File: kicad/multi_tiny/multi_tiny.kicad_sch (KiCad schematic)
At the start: 43 parts, among them J1 Conn_02x04, J2 Conn_02x03_Odd_Even, J3 Conn_01x13, J4 Conn_02x14_Odd_Even, SW1 SW_SPDT, SW2 SW_SPDT, SW3 SW_SPDT, SW4 SW_SPST, U1 CD4052B, U2 CD4052B, U3 CD4052B, U4 CD4052B

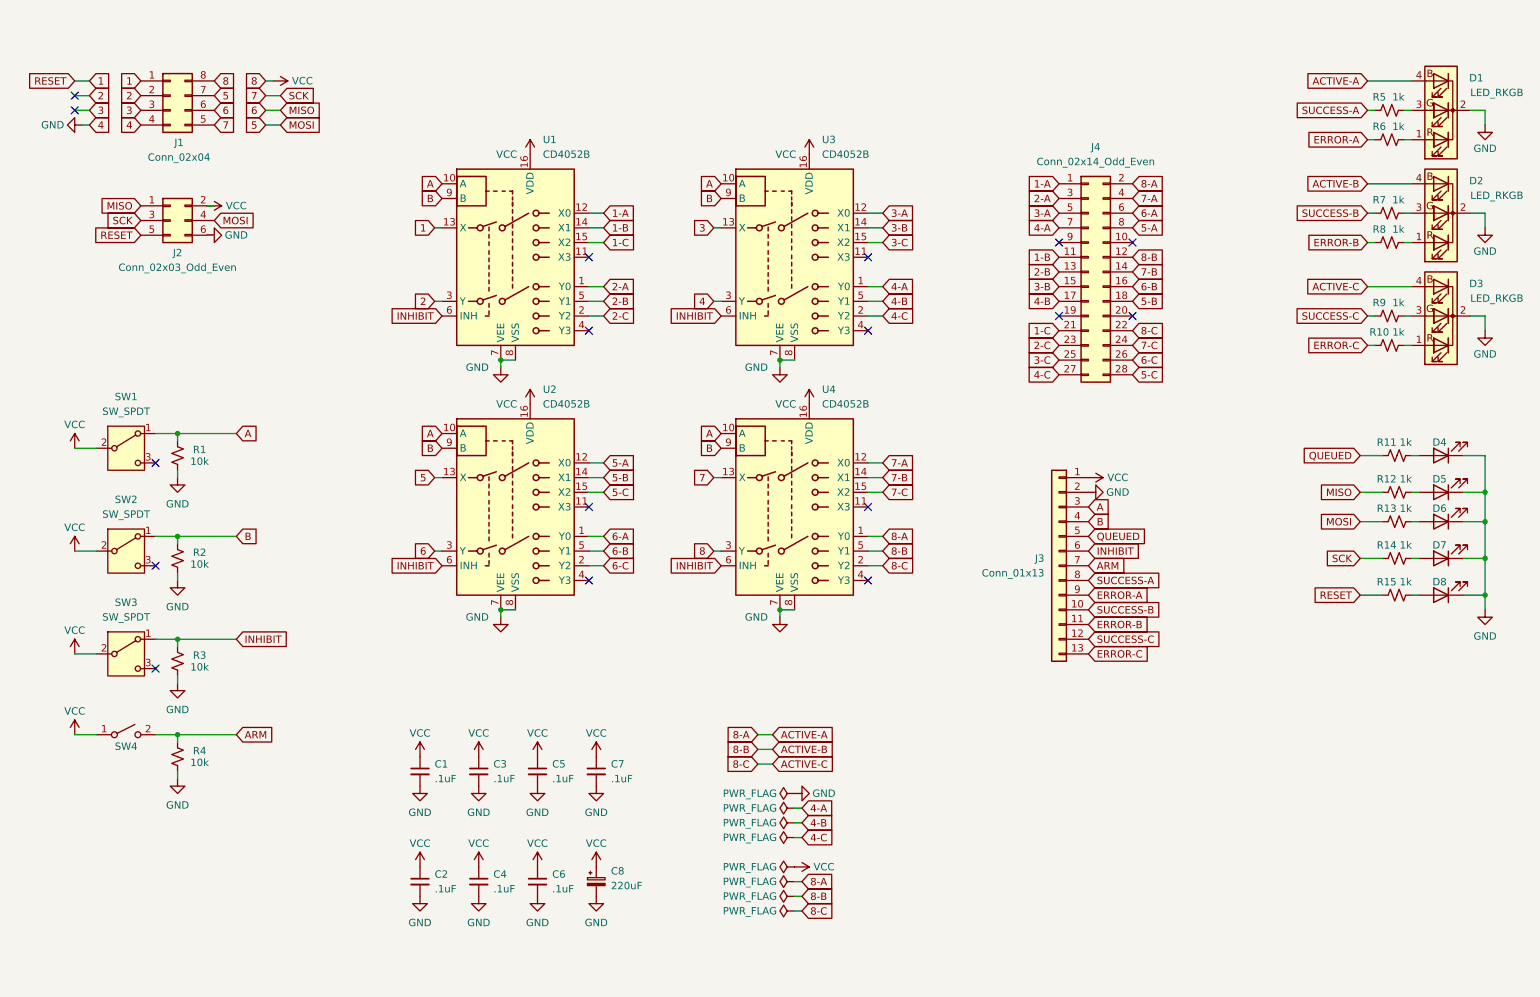
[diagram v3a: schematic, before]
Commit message: Add more IO and organize
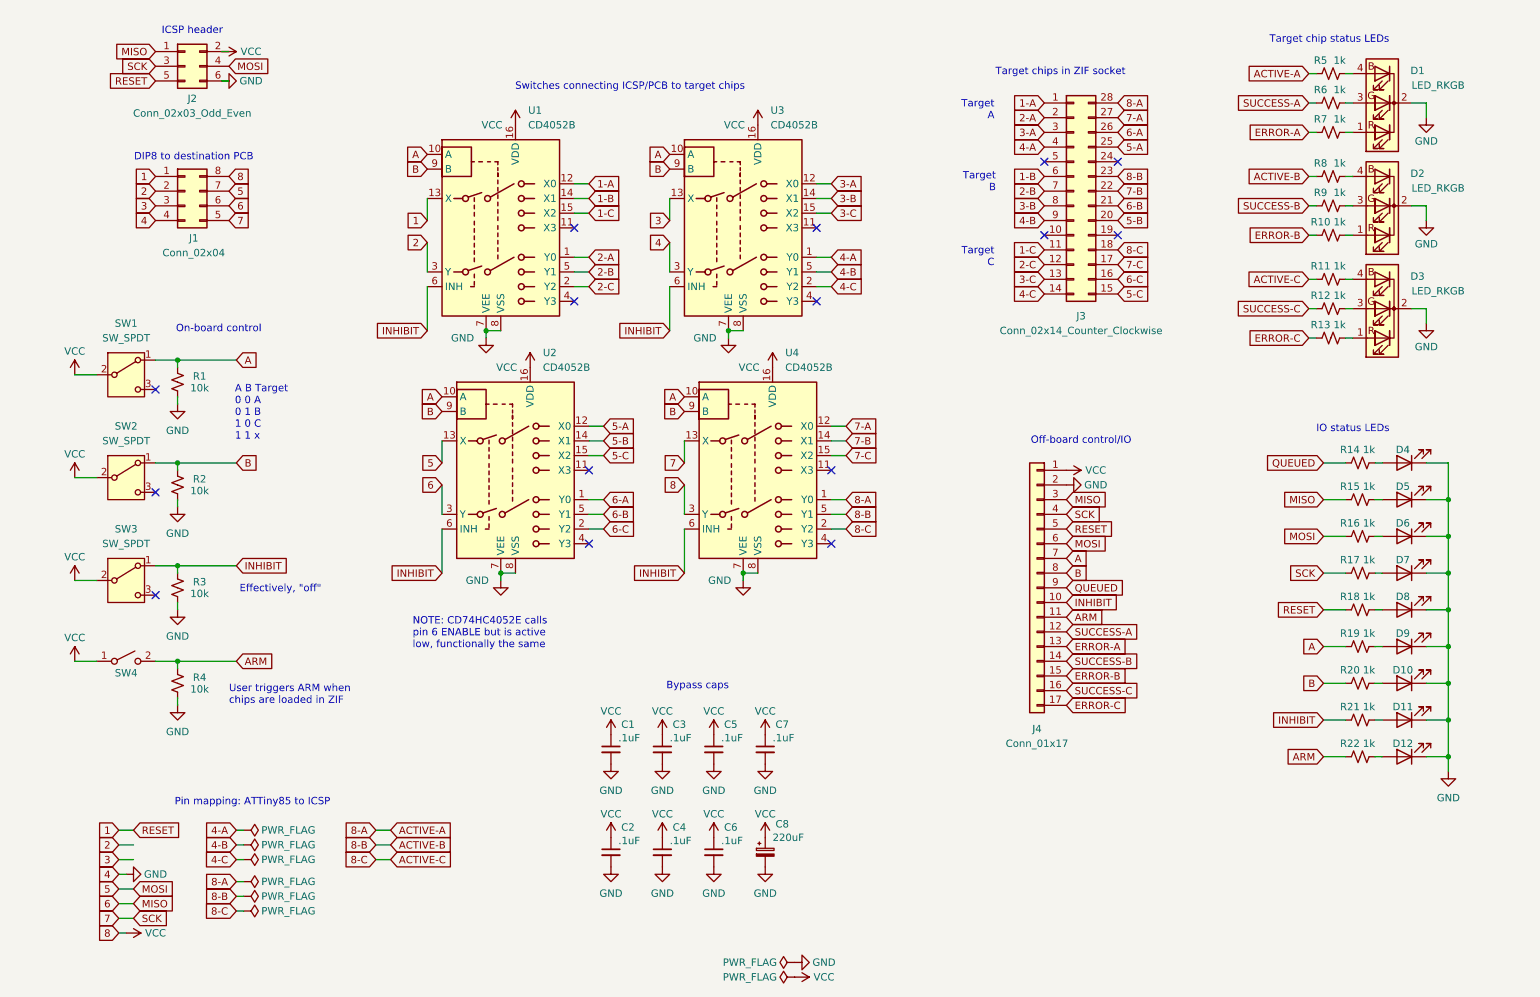
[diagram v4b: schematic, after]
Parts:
- removed J3: Conn_01x13, symbol Connector_Generic:Conn_01x13
- removed J4: Conn_02x14_Odd_Even, symbol Connector_Generic:Conn_02x14_Odd_Even
- added D10, D11, D12, D9: LED, symbol Device:LED
- added J3: Conn_02x14_Counter_Clockwise, symbol Connector_Generic:Conn_02x14_Counter_Clockwise
- added J4: Conn_01x17, symbol Connector_Generic:Conn_01x17
- added R11, R19, R20, R21, R22, R5, R8: 1k, symbol Device:R_Small_US
- renumbered R8 to R10, R9 to R12, R10 to R13, R11 to R14, R12 to R15, R13 to R16, R14 to R17, R15 to R18, R5 to R6, R6 to R7, R7 to R9
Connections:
- net 1: now also J4.5 (Pin_5)
- net 1-A: now also J3.1 (Pin_1)
- net 1-B: now also J3.6 (Pin_6)
- net 1-C: now also J3.11 (Pin_11)
- net 2-A: now also J3.2 (Pin_2)
- net 2-B: now also J3.7 (Pin_7)
- net 2-C: now also J3.12 (Pin_12)
- net 3-A: now also J3.3 (Pin_3)
- net 3-B: now also J3.8 (Pin_8)
- net 3-C: now also J3.13 (Pin_13)
- net 4-A: now also J3.4 (Pin_4)
- net 4-B: now also J3.9 (Pin_9)
- net 4-C: now also J3.14 (Pin_14)
- net 5: now also J4.6 (Pin_6)
- net 5-A: now also J3.25 (Pin_25)
- net 5-B: now also J3.20 (Pin_20)
- net 5-C: now also J3.15 (Pin_15)
- net 6: now also J4.3 (Pin_3)
- net 6-A: now also J3.26 (Pin_26)
- net 6-B: now also J3.21 (Pin_21)
- net 6-C: now also J3.16 (Pin_16)
- net 7: now also J4.4 (Pin_4)
- net 7-A: now also J3.27 (Pin_27)
- net 7-B: now also J3.22 (Pin_22)
- net 7-C: now also J3.17 (Pin_17)
- net 8-A: now also J3.28 (Pin_28), R5.1; no longer D1.4 (BA)
- net 8-B: now also J3.23 (Pin_23), R8.1; no longer D2.4 (BA)
- net 8-C: now also J3.18 (Pin_18), R11.1; no longer D3.4 (BA)
- net A: now also J4.7 (Pin_7), R19.1
- net ARM: now also J4.11 (Pin_11), R22.1
- net B: now also J4.8 (Pin_8), R20.1
- net ERROR-A: now also J4.13 (Pin_13)
- net ERROR-B: now also J4.15 (Pin_15)
- net ERROR-C: now also J4.17 (Pin_17)
- net GND: now also D10.1 (K), D11.1 (K), D12.1 (K), D9.1 (K), J4.2 (Pin_2)
- net INHIBIT: now also J4.10 (Pin_10), R21.1
- net QUEUED: now also J4.9 (Pin_9)
- net SUCCESS-A: now also J4.12 (Pin_12)
- net SUCCESS-B: now also J4.14 (Pin_14)
- net SUCCESS-C: now also J4.16 (Pin_16)
- net VCC: now also J4.1 (Pin_1)
- new net: D12.2 (A), R22.2
- new net: D2.4 (BA), R8.2
- new net: D10.2 (A), R20.2
- new net: D1.4 (BA), R5.2
- new net: D3.4 (BA), R11.2
- new net: D11.2 (A), R21.2
- new net: D9.2 (A), R19.2
- no-connect marks 17 -> 15
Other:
- note added: "A B Target 0 0 A 0 1 B 1 0 C 1 1 x"
- note added: "Bypass caps"
- note added: "DIP8 to destination PCB"
- note added: "Effectively, "off""
- note added: "ICSP header"
- note added: "IO status LEDs"
- note added: "NOTE: CD74HC4052E calls pin 6 ENABLE but is active low, functionally the same"
- note added: "Off-board control/IO"
- note added: "On-board control"
- note added: "Pin mapping: ATTiny85 to ICSP"
- note added: "Switches connecting ICSP/PCB to target chips"
- note added: "Target A"
- note added: "Target B"
- note added: "Target C"
- note added: "Target chip status LEDs"
- note added: "Target chips in ZIF socket"
- note added: "User triggers ARM when chips are loaded in ZIF"
- moved on the sheet: C1, C2, C3, C4, C5, C6, C7, C8, D1, D2, D3, D4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

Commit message: Finalize schematic to start PCB layout
For now!

* Merge DIP8 socket into IO header
* Add "power" LED
* Rearrange some stuff
* Assign footprints
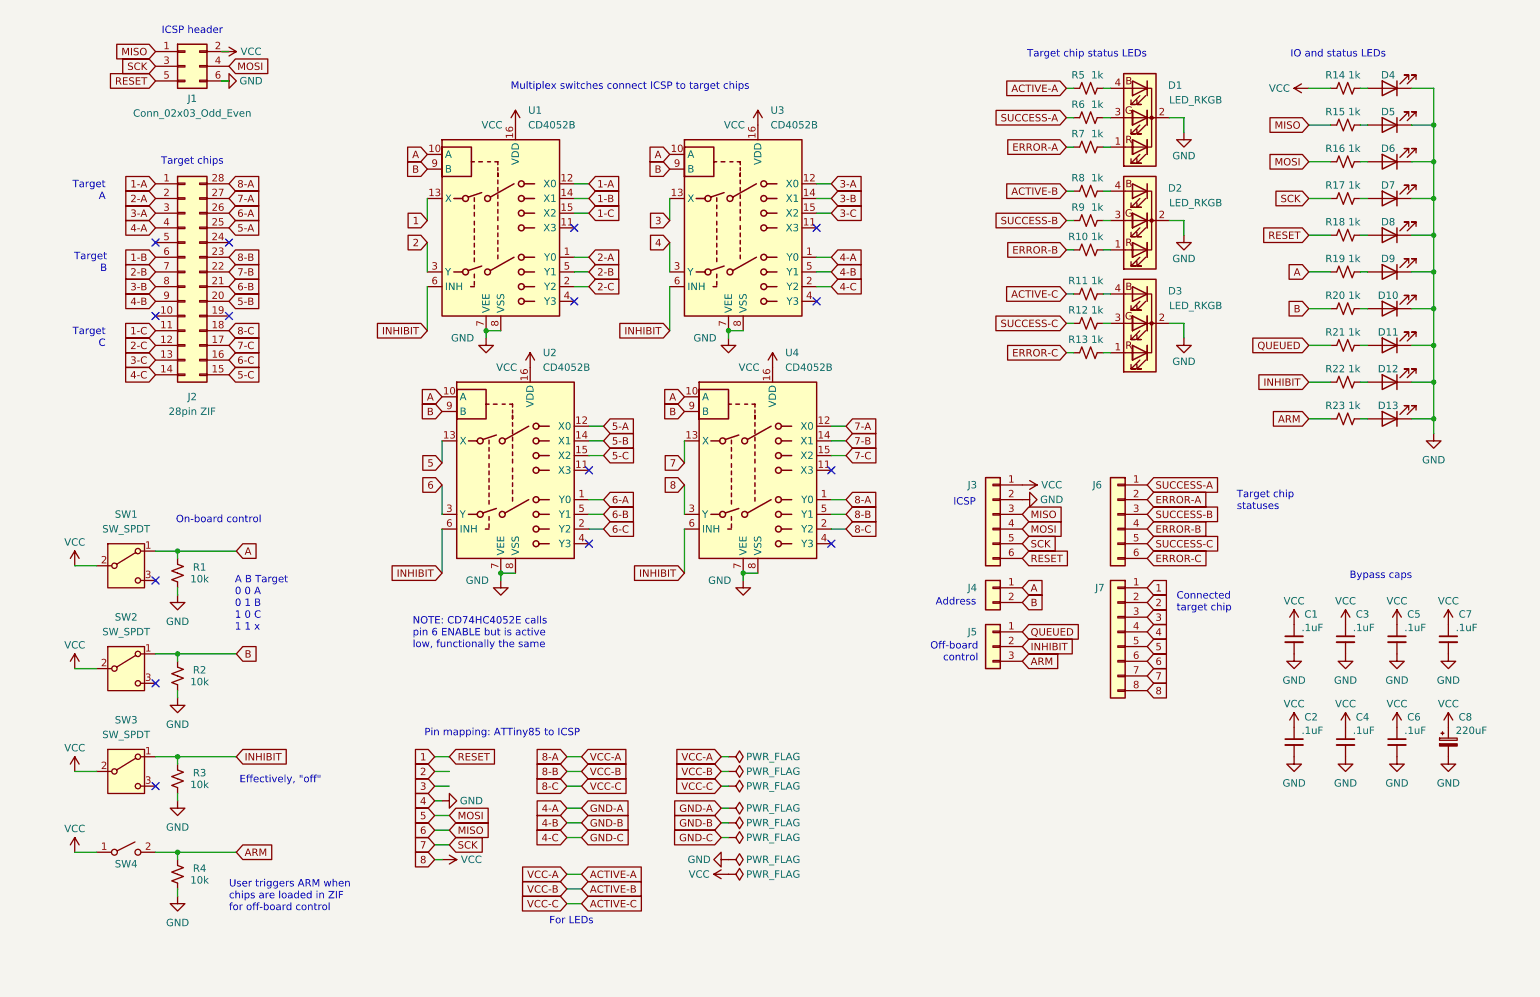
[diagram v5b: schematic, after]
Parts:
- removed J1: Conn_02x04, symbol Connector_Generic:Conn_02x04_Counter_Clockwise
- removed J4: Conn_01x17, symbol Connector_Generic:Conn_01x17
- added D11: LED, LED_THT:LED_D3.0mm, symbol Device:LED
- added J3, J6: DNP, Connector_PinHeader_2.54mm:PinHeader_1x06_P2.54mm_Vertical, symbol Connector_Generic:Conn_01x06
- added J4: DNP, Connector_PinHeader_2.54mm:PinHeader_1x02_P2.54mm_Vertical, symbol Connector_Generic:Conn_01x02
- added J5: DNP, Connector_PinHeader_2.54mm:PinHeader_1x03_P2.54mm_Vertical, symbol Connector_Generic:Conn_01x03
- added J7: DNP, Connector_PinHeader_2.54mm:PinHeader_1x08_P2.54mm_Vertical, symbol Connector_Generic:Conn_01x08
- added R21: 1k, Resistor_THT:R_Axial_DIN0207_L6.3mm_D2.5mm_P10.16mm_Horizontal, symbol Device:R_Small_US
- C1, C2, C3, C4, C5, C6, C7: footprint (none) -> Capacitor_THT:C_Disc_D5.0mm_W2.5mm_P5.00mm
- C8: footprint (none) -> Capacitor_THT:CP_Radial_D8.0mm_P3.50mm
- D1, D2, D3: footprint (none) -> LED_THT:LED_D5.0mm-4_RGB_Staggered_Pins
- D10, D4, D5, D6, D7, D8, D9: footprint (none) -> LED_THT:LED_D3.0mm
- D12: renamed from D11; footprint (none) -> LED_THT:LED_D3.0mm
- D13: renamed from D12; footprint (none) -> LED_THT:LED_D3.0mm
- J1: renamed from J2; footprint (none) -> Connector_PinHeader_2.54mm:PinHeader_2x03_P2.54mm_Vertical
- J2: renamed from J3; value Conn_02x14_Counter_Clockwise -> 28pin ZIF; footprint (none) -> Socket:DIP_Socket-28_W6.9_W7.62_W10.16_W12.7_W13.5_3M_228-4817-00-0602J
- R1, R10, R11, R12, R13, R14, R15, R16, R17, R18, R19, R2, R20, R3, R4, R5, R6, R7, R8, R9: footprint (none) -> Resistor_THT:R_Axial_DIN0207_L6.3mm_D2.5mm_P10.16mm_Horizontal
- R22: renamed from R21; footprint (none) -> Resistor_THT:R_Axial_DIN0207_L6.3mm_D2.5mm_P10.16mm_Horizontal
- R23: renamed from R22; footprint (none) -> Resistor_THT:R_Axial_DIN0207_L6.3mm_D2.5mm_P10.16mm_Horizontal
- SW1, SW2, SW3: footprint (none) -> Button_Switch_THT:SW_Slide_SPDT_Straight_CK_OS102011MS2Q
- SW4: footprint (none) -> Button_Switch_THT:SW_PUSH_6mm
- U1, U2, U3, U4: footprint (none) -> Package_DIP:DIP-16_W7.62mm_Socket_LongPads
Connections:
- net 1: now also J3.6 (Pin_6), J7.1 (Pin_1)
- net 2: now also J7.2 (Pin_2)
- net 3: now also J7.3 (Pin_3)
- net 5: now also J3.4 (Pin_4), J7.5 (Pin_5)
- net 6: now also J3.3 (Pin_3), J7.6 (Pin_6)
- net 7: now also J3.5 (Pin_5), J7.7 (Pin_7)
- net A: now also J4.1 (Pin_1)
- net ARM: now also J5.3 (Pin_3)
- net B: now also J4.2 (Pin_2)
- net ERROR-A: now also J6.2 (Pin_2)
- net ERROR-B: now also J6.4 (Pin_4)
- net ERROR-C: now also J6.6 (Pin_6)
- net GND: now also D11.1 (K), J3.2 (Pin_2), J7.4 (Pin_4)
- net INHIBIT: now also J5.2 (Pin_2)
- net QUEUED: now also J5.1 (Pin_1), R21.1; no longer R14.1
- net SUCCESS-A: now also J6.1 (Pin_1)
- net SUCCESS-B: now also J6.3 (Pin_3)
- net SUCCESS-C: now also J6.5 (Pin_5)
- net VCC: now also R14.1, J3.1 (Pin_1), J7.8 (Pin_8)
- new net: D11.2 (A), R21.2
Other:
- note added: "Address"
- note added: "Connected target chip"
- note added: "For LEDs"
- note added: "ICSP"
- note added: "IO and status LEDs"
- note added: "Multiplex switches connect ICSP to target chips"
- note added: "Off-board control"
- note added: "Target chip statuses"
- note added: "Target chips"
- note added: "User triggers ARM when chips are loaded in ZIF for off-board control"
- note removed: "DIP8 to destination PCB"
- note removed: "IO status LEDs"
- note removed: "Off-board control/IO"
- note removed: "Switches connecting ICSP/PCB to target chips"
- note removed: "Target chips in ZIF socket"
- note removed: "User triggers ARM when chips are loaded in ZIF"
- moved on the sheet: C1, C2, C3, C4, C5, C6, C7, C8, D1, D10, D12, D13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

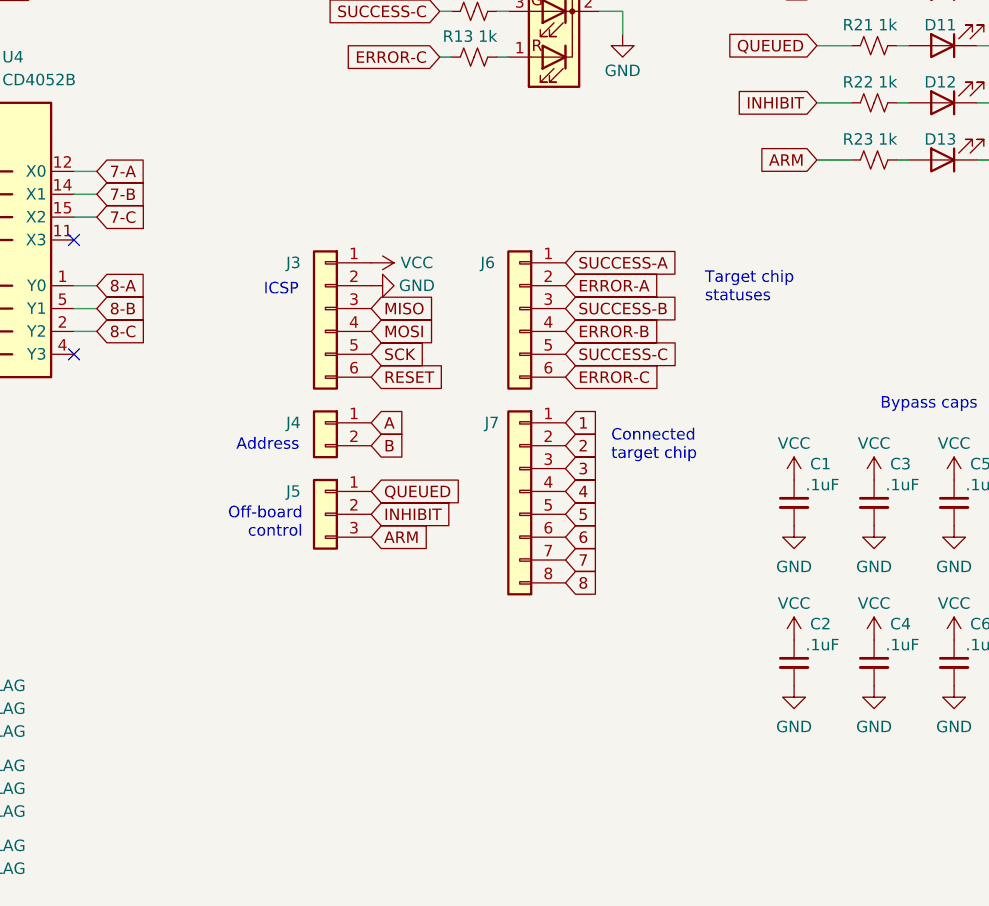
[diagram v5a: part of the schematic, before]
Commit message: Stub PCB layout
Schematic changes are mostly for real estate:

* Combine headers
* Vertical resistors
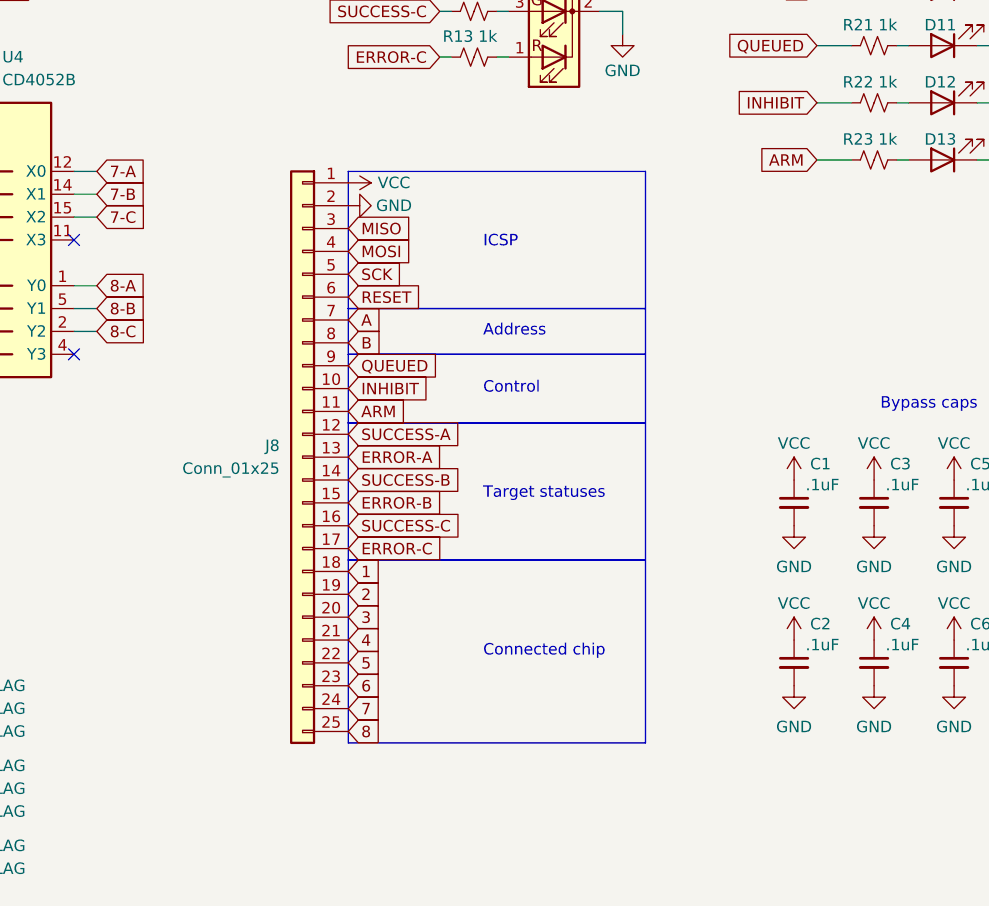
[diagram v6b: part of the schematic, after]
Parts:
- removed J3, J6: DNP, Connector_PinHeader_2.54mm:PinHeader_1x06_P2.54mm_Vertical, symbol Connector_Generic:Conn_01x06
- removed J4: DNP, Connector_PinHeader_2.54mm:PinHeader_1x02_P2.54mm_Vertical, symbol Connector_Generic:Conn_01x02
- removed J5: DNP, Connector_PinHeader_2.54mm:PinHeader_1x03_P2.54mm_Vertical, symbol Connector_Generic:Conn_01x03
- removed J7: DNP, Connector_PinHeader_2.54mm:PinHeader_1x08_P2.54mm_Vertical, symbol Connector_Generic:Conn_01x08
- added J8: Conn_01x25, Connector_PinSocket_2.54mm:PinSocket_1x25_P2.54mm_Vertical, symbol Connector_Generic:Conn_01x25
- D10: value LED -> B
- D11: value LED -> QUEUED
- D12: value LED -> INHIBIT
- D13: value LED -> ARM
- D4: value LED -> VCC
- D5: value LED -> MISO
- D6: value LED -> MOSI
- D7: value LED -> SCK
- D8: value LED -> RESET
- D9: value LED -> A
- R10, R11, R12, R13, R14, R15, R16, R17, R18, R19, R20, R21, R22, R23, R5, R6, R7, R8, R9: footprint Resistor_THT:R_Axial_DIN0207_L6.3mm_D2.5mm_P10.16mm_Horizontal -> Resistor_THT:R_Axial_DIN0207_L6.3mm_D2.5mm_P2.54mm_Vertical
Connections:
- net 1: now also J8.18 (Pin_18), J8.6 (Pin_6)
- net 2: now also J8.19 (Pin_19)
- net 3: now also J8.20 (Pin_20)
- net 5: now also J8.22 (Pin_22), J8.4 (Pin_4)
- net 6: now also J8.23 (Pin_23), J8.3 (Pin_3)
- net 7: now also J8.24 (Pin_24), J8.5 (Pin_5)
- net A: now also J8.7 (Pin_7)
- net ARM: now also J8.11 (Pin_11)
- net B: now also J8.8 (Pin_8)
- net ERROR-A: now also J8.13 (Pin_13)
- net ERROR-B: now also J8.15 (Pin_15)
- net ERROR-C: now also J8.17 (Pin_17)
- net GND: now also J8.2 (Pin_2), J8.21 (Pin_21)
- net INHIBIT: now also J8.10 (Pin_10)
- net QUEUED: now also J8.9 (Pin_9)
- net SUCCESS-A: now also J8.12 (Pin_12)
- net SUCCESS-B: now also J8.14 (Pin_14)
- net SUCCESS-C: now also J8.16 (Pin_16)
- net VCC: now also J8.1 (Pin_1), J8.25 (Pin_25)
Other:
- note added: "Connected chip"
- note added: "Control"
- note added: "Target statuses"
- note removed: "Connected target chip"
- note removed: "Off-board control"
- note removed: "Target chip statuses"
